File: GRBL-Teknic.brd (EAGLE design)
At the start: 53 x 59.7 mm, 8 parts

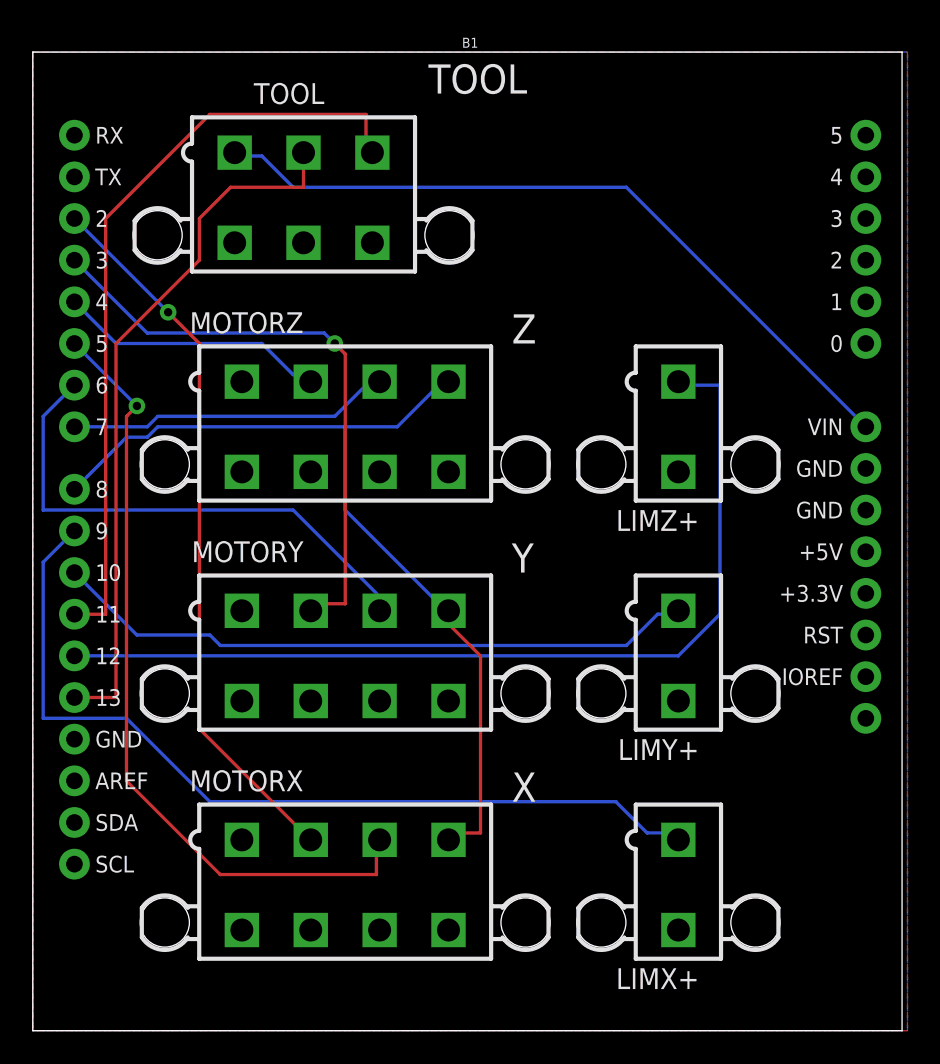
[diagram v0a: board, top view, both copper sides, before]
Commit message: updated with coolant connection
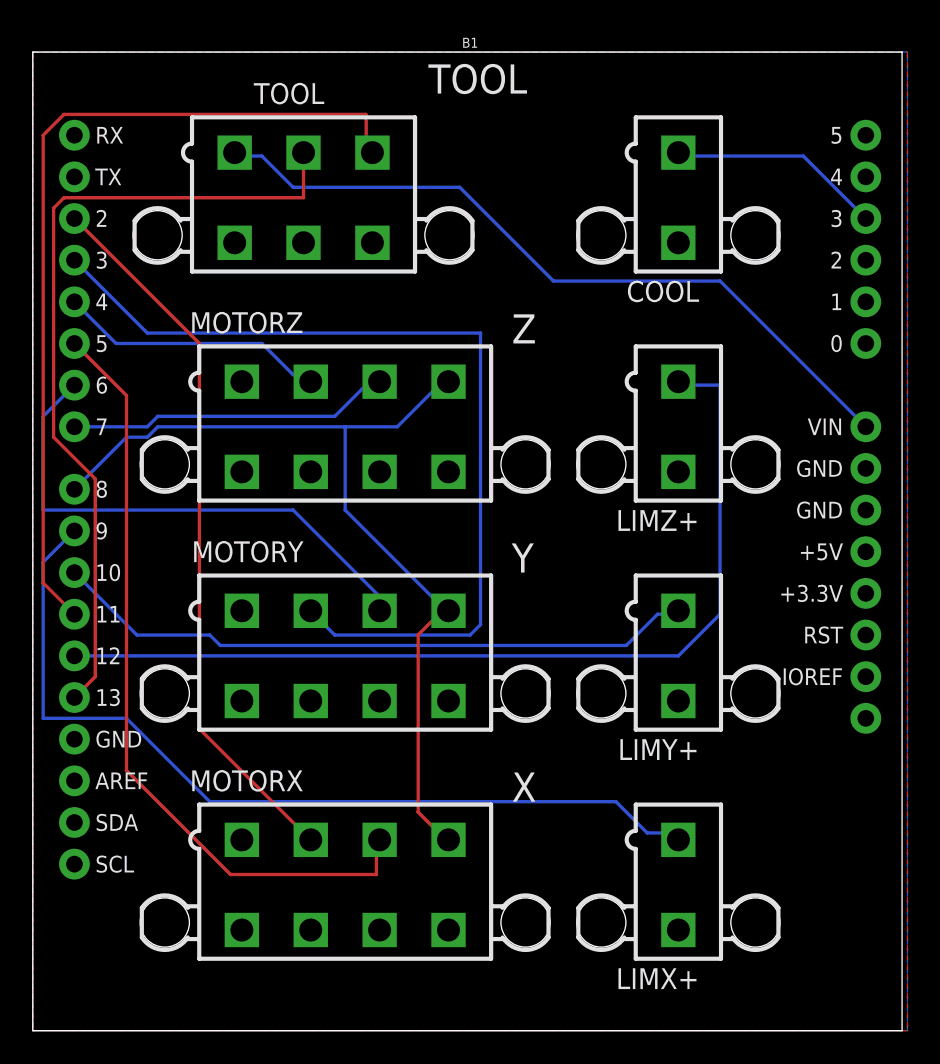
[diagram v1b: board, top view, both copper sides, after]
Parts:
- added COOL: (no value), con-molex-2:5566-2
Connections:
- new net COOL: B1.A3, COOL.1
- net GND: now also B1.GND@1, COOL.2
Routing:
- net STEPY: track 36.5 -> 55.6 mm, vias 1 -> 0
- net COOL: track 0.00 -> 13.2 mm
- net STEPX: track 43.9 -> 51.9 mm, vias 1 -> 0
- net SPINDIR: track 43.1 -> 49.7 mm
- net SPINPWM: track 47.0 -> 52.7 mm
- net DIRZ: track 56.0 -> 55.1 mm
- net DIRX: track 48.3 -> 47.4 mm, vias 1 -> 0
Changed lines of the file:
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@@
 <layers>
 <layer number="1" name="Top" color="4" fill="1" visible="yes" active="yes"/>
-<layer number="16" name="Bottom" color="1" fill="1" visible="yes" active="yes"/>
+<layer number="16" name="Bottom" color="1" fill="1" visible="no" active="yes"/>
 <layer number="17" name="Pads" color="2" fill="1" visible="yes" active="yes"/>
 <layer number="18" name="Vias" color="2" fill="1" visible="yes" active="yes"/>
@@
 <element name="MOTORZ" library="con-molex-2" package="5566-8" value="" x="19.05" y="36.83" rot="R180"/>
 <element name="TOOL" library="con-molex-2" package="5566-6" value="" x="16.51" y="50.8" rot="R180"/>
+<element name="COOL" library="con-molex-2" package="5566-2" value="" x="39.37" y="50.8" rot="R180"/>
 </elements>
 <signals>
@@
 <vertex x="0" y="0"/>
 </polygon>
+<contactref element="COOL" pad="2"/>
+<contactref element="B1" pad="GND@1"/>
 </signal>
 <signal name="VIN">
 <contactref element="B1" pad="VIN"/>
 <contactref element="TOOL" pad="1"/>
-<wire x1="36.195" y1="51.435" x2="50.8" y2="36.83" width="0.2032" layer="16"/>
-<wire x1="15.875" y1="51.435" x2="36.195" y2="51.435" width="0.2032" layer="16"/>
+<wire x1="41.91" y1="45.72" x2="50.8" y2="36.83" width="0.2032" layer="16"/>
+<wire x1="31.75" y1="45.72" x2="41.91" y2="45.72" width="0.2032" layer="16"/>
+<wire x1="26.035" y1="51.435" x2="31.75" y2="45.72" width="0.2032" layer="16"/>
+<wire x1="15.875" y1="51.435" x2="26.035" y2="51.435" width="0.2032" layer="16"/>
 <wire x1="13.97" y1="53.34" x2="15.875" y2="51.435" width="0.2032" layer="16"/>
 <wire x1="12.7" y1="53.34" x2="13.97" y2="53.34" width="0.2032" layer="16"/>
@@
 <contactref element="B1" pad="D13"/>
 <contactref element="TOOL" pad="2"/>
-<wire x1="5.08" y1="20.32" x2="2.54" y2="20.32" width="0.2032" layer="1"/>
-<wire x1="5.08" y1="41.91" x2="5.08" y2="20.32" width="0.2032" layer="1"/>
-<wire x1="10.16" y1="46.99" x2="5.08" y2="41.91" width="0.2032" layer="1"/>
-<wire x1="10.16" y1="49.53" x2="10.16" y2="46.99" width="0.2032" layer="1"/>
-<wire x1="12.065" y1="51.435" x2="10.16" y2="49.53" width="0.2032" layer="1"/>
-<wire x1="16.51" y1="51.435" x2="12.065" y2="51.435" width="0.2032" layer="1"/>
-<wire x1="16.51" y1="53.55" x2="16.51" y2="51.435" width="0.2032" layer="1"/>
+<wire x1="3.81" y1="21.59" x2="2.54" y2="20.32" width="0.2032" layer="1"/>
+<wire x1="3.81" y1="33.655" x2="3.81" y2="21.59" width="0.2032" layer="1"/>
+<wire x1="1.27" y1="36.195" x2="3.81" y2="33.655" width="0.2032" layer="1"/>
+<wire x1="1.27" y1="50.165" x2="1.27" y2="36.195" width="0.2032" layer="1"/>
+<wire x1="1.905" y1="50.8" x2="1.27" y2="50.165" width="0.2032" layer="1"/>
+<wire x1="16.51" y1="50.8" x2="1.905" y2="50.8" width="0.2032" layer="1"/>
+<wire x1="16.51" y1="53.55" x2="16.51" y2="50.8" width="0.2032" layer="1"/>
 </signal>
 <signal name="SPINPWM">
 <contactref element="B1" pad="D11"/>
 <contactref element="TOOL" pad="3"/>
-<wire x1="4.445" y1="25.4" x2="2.54" y2="25.4" width="0.2032" layer="1"/>
-<wire x1="4.445" y1="49.53" x2="4.445" y2="25.4" width="0.2032" layer="1"/>
-<wire x1="10.795" y1="55.88" x2="4.445" y2="49.53" width="0.2032" layer="1"/>
-<wire x1="20.32" y1="55.88" x2="10.795" y2="55.88" width="0.2032" layer="1"/>
+<wire x1="0.635" y1="27.305" x2="2.54" y2="25.4" width="0.2032" layer="1"/>
+<wire x1="0.635" y1="54.61" x2="0.635" y2="27.305" width="0.2032" layer="1"/>
+<wire x1="1.905" y1="55.88" x2="0.635" y2="54.61" width="0.2032" layer="1"/>
+<wire x1="20.32" y1="55.88" x2="1.905" y2="55.88" width="0.2032" layer="1"/>
 <wire x1="20.32" y1="53.975" x2="20.32" y2="55.88" width="0.2032" layer="1"/>
 <wire x1="20.32" y1="53.975" x2="20.71" y2="53.55" width="0.2032" layer="1"/>
@@
 <wire x1="10.16" y1="18.415" x2="16.51" y2="12.065" width="0.2032" layer="1"/>
 <wire x1="10.16" y1="41.91" x2="10.16" y2="18.415" width="0.2032" layer="1"/>
-<wire x1="8.255" y1="43.815" x2="10.16" y2="41.91" width="0.2032" layer="1"/>
+<wire x1="2.54" y1="49.53" x2="10.16" y2="41.91" width="0.2032" layer="1"/>
 <wire x1="16.51" y1="12.065" x2="16.95" y2="11.64" width="0.2032" layer="1"/>
-<via x="8.255" y="43.815" extent="1-16" drill="0.508"/>
 </signal>
 <signal name="STEPY">
@@
 <contactref element="B1" pad="D3"/>
 <wire x1="6.985" y1="42.545" x2="2.54" y2="46.99" width="0.2032" layer="16"/>
-<wire x1="17.78" y1="42.545" x2="6.985" y2="42.545" width="0.2032" layer="16"/>
-<wire x1="19.05" y1="26.035" x2="17.145" y2="26.035" width="0.2032" layer="1"/>
-<wire x1="19.05" y1="41.275" x2="19.05" y2="26.035" width="0.2032" layer="1"/>
-<wire x1="18.415" y1="41.91" x2="19.05" y2="41.275" width="0.2032" layer="1"/>
-<wire x1="17.78" y1="42.545" x2="18.415" y2="41.91" width="0.2032" layer="16"/>
-<wire x1="17.145" y1="26.035" x2="16.95" y2="25.61" width="0.2032" layer="1"/>
-<via x="18.415" y="41.91" extent="1-16" drill="0.508"/>
+<wire x1="27.305" y1="42.545" x2="6.985" y2="42.545" width="0.2032" layer="16"/>
+<wire x1="18.415" y1="24.13" x2="17.145" y2="25.4" width="0.2032" layer="16"/>
+<wire x1="26.67" y1="24.13" x2="18.415" y2="24.13" width="0.2032" layer="16"/>
+<wire x1="27.305" y1="24.765" x2="26.67" y2="24.13" width="0.2032" layer="16"/>
+<wire x1="27.305" y1="42.545" x2="27.305" y2="24.765" width="0.2032" layer="16"/>
+<wire x1="17.145" y1="25.4" x2="16.95" y2="25.61" width="0.2032" layer="16"/>
 </signal>
 <signal name="STEPZ">
@@
 <contactref element="MOTORX" pad="3"/>
 <contactref element="B1" pad="D5"/>
-<wire x1="6.35" y1="38.1" x2="2.54" y2="41.91" width="0.2032" layer="16"/>
-<wire x1="5.715" y1="37.465" x2="6.35" y2="38.1" width="0.2032" layer="1"/>
-<wire x1="5.715" y1="15.24" x2="5.715" y2="37.465" width="0.2032" layer="1"/>
-<wire x1="11.43" y1="9.525" x2="5.715" y2="15.24" width="0.2032" layer="1"/>
-<wire x1="20.955" y1="9.525" x2="11.43" y2="9.525" width="0.2032" layer="1"/>
+<wire x1="5.715" y1="38.735" x2="2.54" y2="41.91" width="0.2032" layer="1"/>
+<wire x1="5.715" y1="15.875" x2="5.715" y2="38.735" width="0.2032" layer="1"/>
+<wire x1="12.065" y1="9.525" x2="5.715" y2="15.875" width="0.2032" layer="1"/>
+<wire x1="20.955" y1="9.525" x2="12.065" y2="9.525" width="0.2032" layer="1"/>
 <wire x1="20.955" y1="11.43" x2="20.955" y2="9.525" width="0.2032" layer="1"/>
 <wire x1="20.955" y1="11.43" x2="21.15" y2="11.64" width="0.2032" layer="1"/>
-<via x="6.35" y="38.1" extent="1-16" drill="0.508"/>
 </signal>
 <signal name="DIRY">
@@
 <wire x1="19.05" y1="36.83" x2="19.05" y2="31.75" width="0.2032" layer="16"/>
 <wire x1="24.765" y1="26.035" x2="25.35" y2="25.61" width="0.2032" layer="16"/>
-<wire x1="27.305" y1="12.065" x2="25.4" y2="12.065" width="0.2032" layer="1"/>
-<wire x1="27.305" y1="22.86" x2="27.305" y2="12.065" width="0.2032" layer="1"/>
-<wire x1="25.4" y1="24.765" x2="27.305" y2="22.86" width="0.2032" layer="1"/>
-<wire x1="25.4" y1="25.4" x2="25.4" y2="24.765" width="0.2032" layer="1"/>
-<wire x1="25.4" y1="12.065" x2="25.35" y2="11.64" width="0.2032" layer="1"/>
-<wire x1="25.4" y1="25.4" x2="25.35" y2="25.61" width="0.2032" layer="1"/>
+<wire x1="23.495" y1="13.335" x2="24.765" y2="12.065" width="0.2032" layer="1"/>
+<wire x1="23.495" y1="24.13" x2="23.495" y2="13.335" width="0.2032" layer="1"/>
+<wire x1="24.765" y1="25.4" x2="23.495" y2="24.13" width="0.2032" layer="1"/>
+<wire x1="24.765" y1="12.065" x2="25.35" y2="11.64" width="0.2032" layer="1"/>
+<wire x1="24.765" y1="25.4" x2="25.35" y2="25.61" width="0.2032" layer="1"/>
+</signal>
+<signal name="COOL">
+<contactref element="COOL" pad="1"/>
+<contactref element="B1" pad="A3"/>
+<wire x1="46.99" y1="53.34" x2="50.8" y2="49.53" width="0.2032" layer="16"/>
+<wire x1="39.37" y1="53.34" x2="46.99" y2="53.34" width="0.2032" layer="16"/>
+<wire x1="39.37" y1="53.34" x2="39.37" y2="53.55" width="0.2032" layer="16"/>
 </signal>
 </signals>

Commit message: designed multi direction limit switch
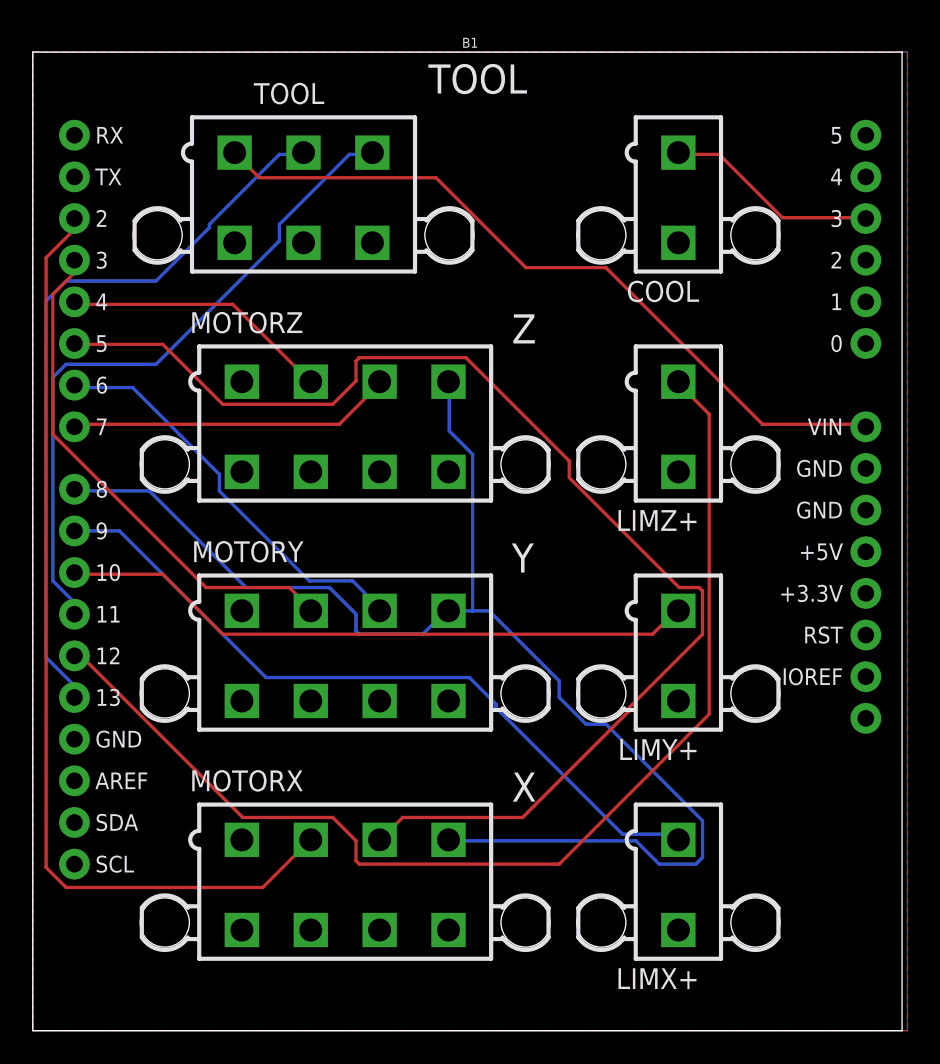
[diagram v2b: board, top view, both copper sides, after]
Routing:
- net DIRX: track 47.4 -> 75.8 mm
- net DIRZ: track 55.1 -> 82.1 mm
- net STEPY: track 55.6 -> 31.4 mm
- net LIMZ: track 57.1 -> 69.5 mm
- net SPINPWM: track 52.7 -> 40.8 mm
- net LIMX: track 54.3 -> 44.8 mm
- net DIRY: track 32.3 -> 25.0 mm
- net STEPX: track 51.9 -> 58.1 mm
- net SPINDIR: track 49.7 -> 44.5 mm
- net LIMY: track 39.7 -> 39.0 mm
- added copper zone on layer 1, net VIN
- removed copper zone on layer 1, net GND

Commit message: updated as I learn more from EMI filtering
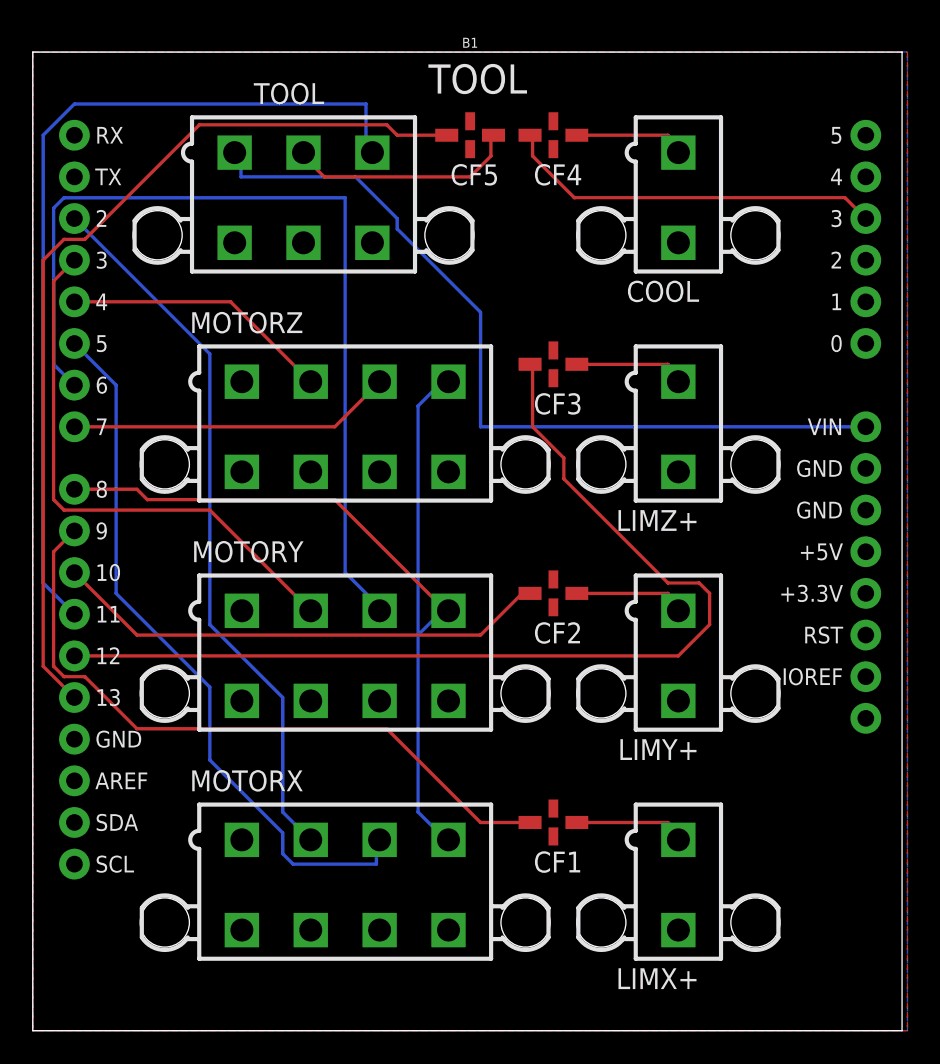
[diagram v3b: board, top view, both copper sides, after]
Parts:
- added CF1, CF2, CF3, CF4, CF5: NFM21C, murata-filter:NFM21C
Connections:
- removed net N$6: B1.D7, MOTORZ.3
- new net ENABLE: B1.D8, MOTORX.4, MOTORY.4, MOTORZ.4
- new net N$1: CF4.1, COOL.1
- new net N$2: CF5.1, TOOL.2
- new net N$3: CF1.1, LIMX+.1
- new net N$4: CF2.1, LIMY+.1
- new net N$5: CF3.1, LIMZ+.1
- net COOL: now also CF4.3; no longer COOL.1
- net DIRZ: now also B1.D7, MOTORZ.3; no longer B1.D8, MOTORX.4, MOTORY.4, MOTORZ.4
- net GND: now also CF1.2@1, CF2.2@1, CF3.2@1, CF4.2@1, CF5.2@1
- net LIMX: now also CF1.3; no longer LIMX+.1
- net LIMY: now also CF2.3; no longer LIMY+.1
- net LIMZ: now also CF3.3; no longer LIMZ+.1
- net SPINDIR: now also CF5.3; no longer TOOL.2
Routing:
- net DIRZ: track 82.1 -> 19.8 mm
- net ENABLE: track 0.00 -> 58.0 mm
- net DIRX: track 75.8 -> 43.9 mm
- net DIRY: track 25.0 -> 55.4 mm
- net N$6: track 19.8 -> 0.00 mm
- net STEPX: track 58.1 -> 43.9 mm
- net N$2: track 0.00 -> 14.1 mm
- net SPINPWM: track 40.8 -> 53.6 mm
- net SPINDIR: track 44.5 -> 55.8 mm
- net COOL: track 13.1 -> 23.3 mm
- net LIMY: track 39.0 -> 30.4 mm
- net LIMZ: track 69.5 -> 61.1 mm
- net N$5: track 0.00 -> 6.88 mm
- net N$1: track 0.00 -> 6.88 mm
- net N$4: track 0.00 -> 6.88 mm
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- added copper zone on layer 1, net GND
- removed copper zone on layer 1, net VIN
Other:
- board text removed: "X"
- board text removed: "Y"
- board text removed: "Z"
